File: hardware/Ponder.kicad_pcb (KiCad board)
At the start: 2 copper layers, 40 x 50 mm, 119 parts, among them J1 USB_C_Receptacle_USB2.0, J10 1.27 HDR, J11 2.54 SKT, J12 2.54 SKT, J2 2.54 HDR, J3 2.54 HDR, J4 2.54 HDR, J5 2.54 HDR, J6 2.54 HDR, J7 2.54 HDR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

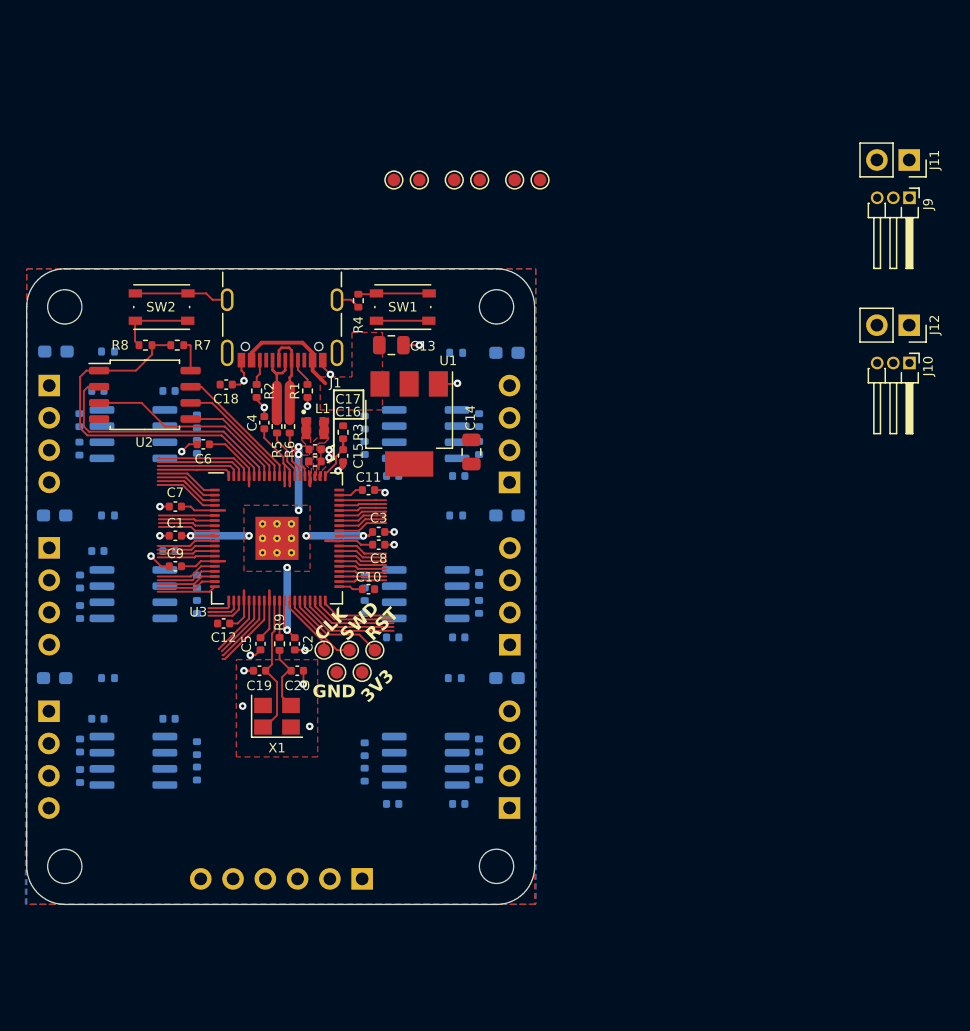
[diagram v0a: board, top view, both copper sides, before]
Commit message: Adding LEDs for power status
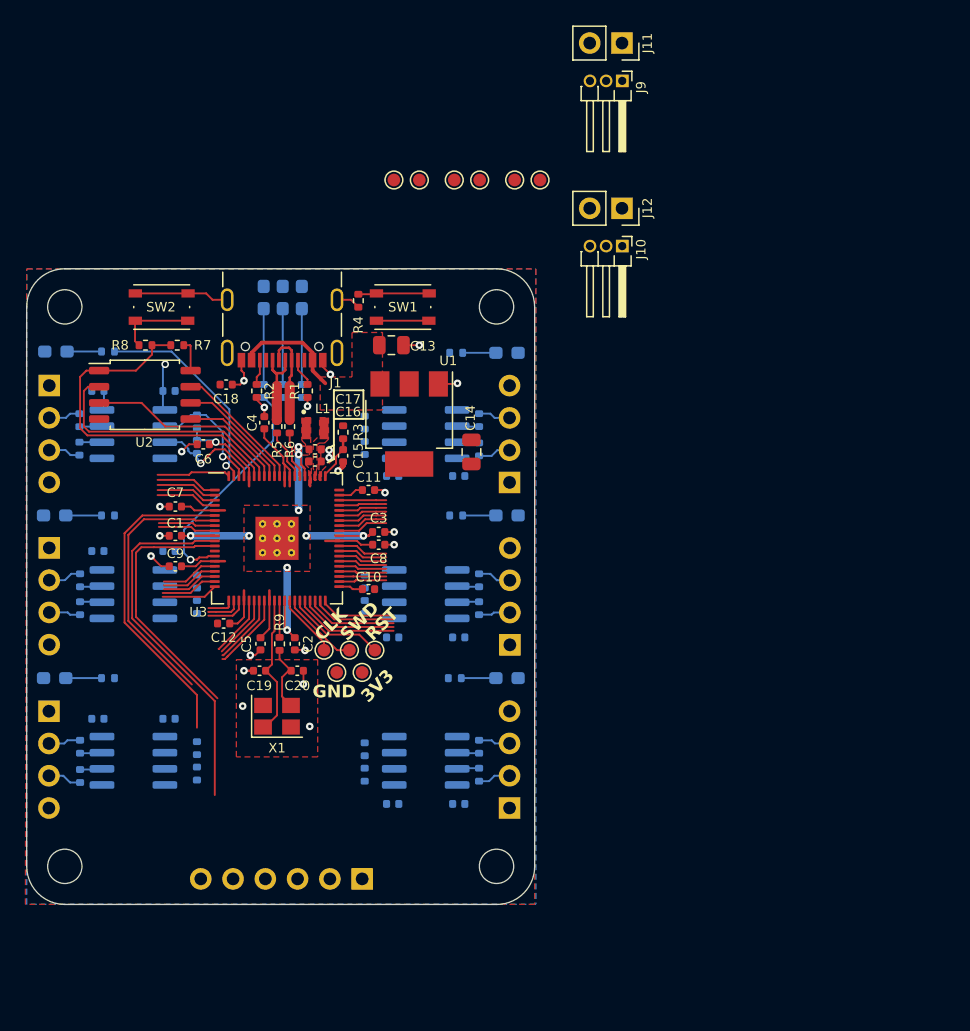
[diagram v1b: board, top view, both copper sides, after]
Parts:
- added D7: LED, LED_SMD:LED_0603_1608Metric_Pad1.05x0.95mm_HandSolder, B.Cu at (139.2, 75.2)
- added D8: LED, LED_SMD:LED_0603_1608Metric_Pad1.05x0.95mm_HandSolder, B.Cu at (140.8, 75.2)
- added D9: LED, LED_SMD:LED_0603_1608Metric_Pad1.05x0.95mm_HandSolder, B.Cu at (142.2, 75.2)
- added R40: 1k, Resistor_SMD:R_0402_1005Metric, B.Cu at (139.2, 82.6)
- added R41: 1k, Resistor_SMD:R_0402_1005Metric, B.Cu at (140.8, 82.6)
- added R42: 1k, Resistor_SMD:R_0402_1005Metric, B.Cu at (142.2, 82.6)
- moved J11 24.4 mm to (167.4, 55.2)
- moved J12 24.4 mm to (167.4, 68.2)
- moved J10 24.4 mm to (167.5, 71.2)
- moved J9 24.4 mm to (167.5, 58.2)
- moved R13 0.30 mm to (124.8, 99.7)
- moved R18 0.11 mm to (156.2, 99.7)
- moved R19 0.11 mm to (156.2, 97.5)
- moved R20 0.11 mm to (156.2, 87.2)
- moved R12 0.10 mm to (124.8, 97.5)
- moved R16 0.10 mm to (156.2, 112.8)
- moved R17 0.10 mm to (156.2, 110.6)
- moved R14 0.09 mm to (124.8, 110.6)
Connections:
- U3 pad 1: /GPIO4 -> /RP_UART1_TX
- U3 pad 11: /GPIO12 -> /RP_UART3_TX
- U3 pad 12: /GPIO13 -> /RP_UART3_RX
- U3 pad 13: /GPIO14 -> unconnected-(U3-GPIO14-Pad13)
- U3 pad 14: /GPIO15 -> /RP_PWR_LED
- U3 pad 16: /GPIO16 -> /RP_UART4_TX
- U3 pad 17: /GPIO17 -> /RP_UART4_RX
- U3 pad 18: /GPIO18 -> /RP_UART4_LED
- U3 pad 19: /GPIO19 -> /RP_UART5_LED
- U3 pad 2: /GPIO5 -> /RP_UART1_RX
- U3 pad 20: /GPIO20 -> /RP_UART5_TX
- U3 pad 21: /GPIO21 -> /RP_UART5_RX
- U3 pad 22: /GPIO22 -> unconnected-(U3-GPIO22-Pad22)
- U3 pad 23: /GPIO23 -> unconnected-(U3-GPIO23-Pad23)
- U3 pad 25: /GPIO24 -> /RP_SPI1-MISO_I2C0-SDA
- U3 pad 26: /GPIO25 -> /RP_SPI1-CSn_I2C0-SCL
- U3 pad 27: /GPIO26 -> /RP_SPI1-SCK_I2C1-SDA
- U3 pad 28: /GPIO27 -> /RP_SPI1-MOSI_I2C1-SCL
- U3 pad 3: /GPIO6 -> unconnected-(U3-GPIO6-Pad3)
- U3 pad 36: /GPIO28 -> unconnected-(U3-GPIO28-Pad36)
- U3 pad 37: /GPIO29 -> unconnected-(U3-GPIO29-Pad37)
- U3 pad 38: /GPIO30 -> unconnected-(U3-GPIO30-Pad38)
- U3 pad 39: /GPIO31 -> unconnected-(U3-GPIO31-Pad39)
- U3 pad 4: /GPIO7 -> unconnected-(U3-GPIO7-Pad4)
- U3 pad 40: /GPIO32 -> unconnected-(U3-GPIO32-Pad40)
- U3 pad 42: /GPIO33 -> unconnected-(U3-GPIO33-Pad42)
- U3 pad 43: /GPIO34 -> unconnected-(U3-GPIO34-Pad43)
- U3 pad 44: /GPIO35 -> unconnected-(U3-GPIO35-Pad44)
- U3 pad 45: /GPIO36 -> unconnected-(U3-GPIO36-Pad45)
- U3 pad 46: /GPIO37 -> unconnected-(U3-GPIO37-Pad46)
- U3 pad 47: /GPIO38 -> unconnected-(U3-GPIO38-Pad47)
- U3 pad 48: /GPIO39 -> unconnected-(U3-GPIO39-Pad48)
- U3 pad 6: /GPIO8 -> /RP_UART2_TX
- U3 pad 7: /GPIO9 -> /RP_UART2_RX
- U3 pad 77: /GPIO0 -> /RP_UART0_TX
- U3 pad 78: /GPIO1 -> /RP_UART0_RX
- U3 pad 79: /GPIO2 -> /RP_UART0_LED
- U3 pad 8: /GPIO10 -> /RP_UART2_LED
- U3 pad 80: /GPIO3 -> /RP_UART1_LED
- U3 pad 9: /GPIO11 -> /RP_UART3_LED
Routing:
- net /RP_UART3_TX: track 0.00 -> 28.7 mm
- net /RP_UART2_TX: track 0.00 -> 25.3 mm
- net /RP_UART2_RX: track 0.00 -> 21.2 mm
- net /RP_UART3_RX: track 0.00 -> 20.5 mm
- net /RP_PWR_LED: track 0.00 -> 18.2 mm, vias 0 -> 1
- net /RP_UART0_LED: track 0.00 -> 16.6 mm, vias 0 -> 1
- net /RP_UART0_RX: track 0.00 -> 9.64 mm, vias 0 -> 1
- net /RP_UART0_TX: track 0.00 -> 8.98 mm, vias 0 -> 1
- net unconnected-(U3-GPIO28-Pad36): track 0.00 -> 8.25 mm
- net /GPIO28: track 8.25 -> 0.00 mm
- net /GPIO0: track 7.73 -> 0.00 mm
- net unconnected-(U3-GPIO29-Pad37): track 0.00 -> 7.72 mm
- net /GPIO29: track 7.72 -> 0.00 mm
- net /GPIO1: track 7.20 -> 0.00 mm
- net unconnected-(U3-GPIO30-Pad38): track 0.00 -> 7.18 mm
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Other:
- board text added: "POWER"

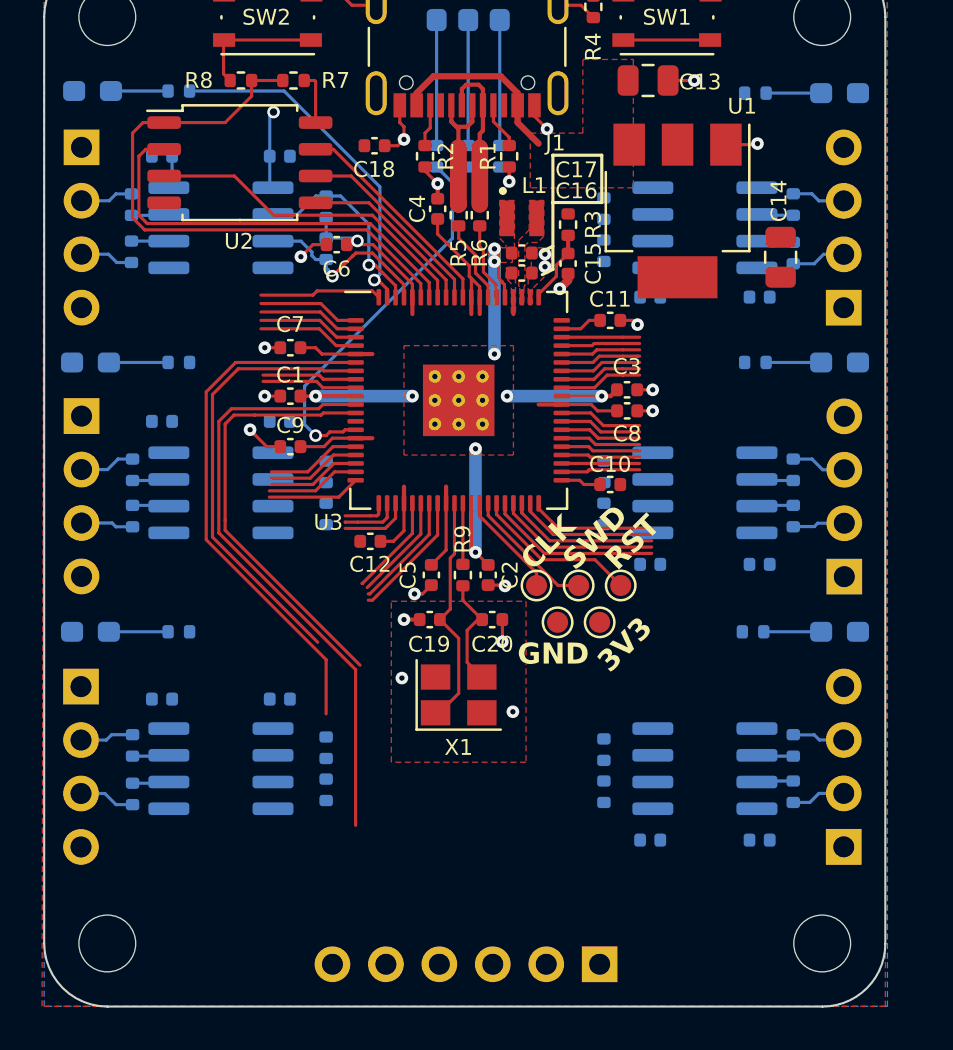
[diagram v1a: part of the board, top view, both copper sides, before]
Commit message: Tittivating connector legends
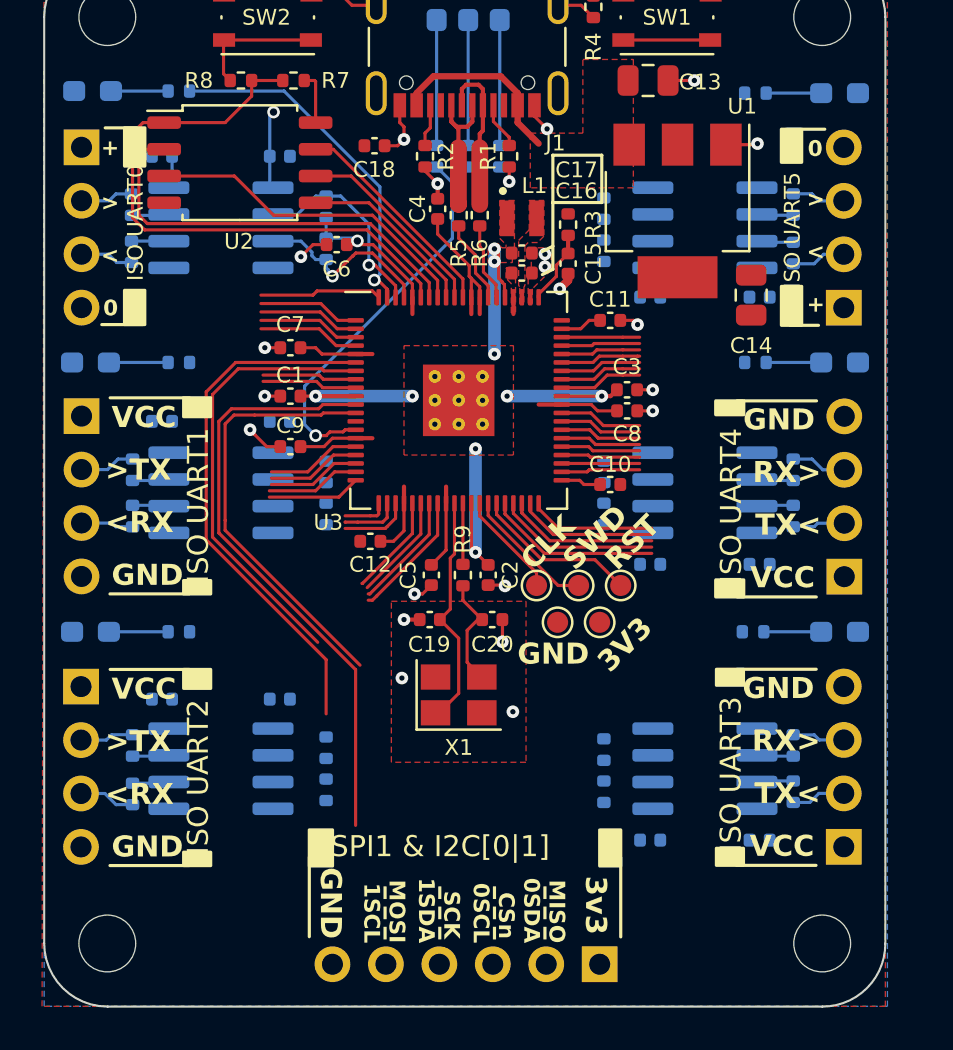
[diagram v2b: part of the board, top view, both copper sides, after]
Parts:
- moved C14 2.28 mm to (154.2, 89.2), turned to -90 degrees
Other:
- board text added: "+"
- board text added: "0"
- board text added: "0SCL"
- board text added: "0SDA"
- board text added: "1SCL"
- board text added: "1SDA"
- board text added: "3v3"
- board text added: "<"
- board text added: "<RX"
- board text added: ">"
- board text added: ">TX"
- board text added: "CSn"
- board text added: "ISO UART0"
- board text added: "ISO UART1"
- board text added: "ISO UART2"
- board text added: "ISO UART3"
- board text added: "ISO UART4"
- board text added: "ISO UART5"
- board text added: "MISO"
- board text added: "MOSI"
- board text added: "RX>"
- board text added: "SCK"
- board text added: "SPI1 & I2C[0|1]"
- board text added: "TX<"
- board text added: "VCC"

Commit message: Minor tweaks an bit of layout
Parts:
- moved R30 2.31 mm to (134.0, 110.4), turned to 90 degrees
- moved C14 2.02 mm to (153.1, 90.9), turned to 0 degrees
- moved R29 2.00 mm to (134.0, 112.7), turned to -90 degrees
- moved C12 0.71 mm to (136.2, 101.6), turned to -135 degrees
- moved C5 0.61 mm to (138.9, 103.1)
- moved C31 0.41 mm to (155.0, 101.9), turned to 0 degrees
- moved C32 0.41 mm to (155.0, 89.2), turned to 0 degrees
- moved C28 0.40 mm to (155.0, 115.1), turned to 0 degrees
- moved R20 0.10 mm to (156.3, 87.2)
- moved R21 0.10 mm to (156.3, 84.9)
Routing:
- net +3V3: track 45.2 -> 73.0 mm, vias 2 -> 12
- net /RP_SPI1-MISO_I2C0-SDA: track 4.81 -> 29.5 mm, vias 0 -> 1
- net /RP_SPI1-CSn_I2C0-SCL: track 5.06 -> 27.3 mm, vias 0 -> 1
- net /RP_SPI1-SCK_I2C1-SDA: track 5.55 -> 25.9 mm, vias 0 -> 1
- net /RP_SPI1-MOSI_I2C1-SCL: track 6.09 -> 24.0 mm
- net /RP_UART3_TX: track 28.7 -> 14.8 mm
- net /RP_UART1_TX: track 4.83 -> 16.1 mm, vias 0 -> 1
- net /RP_UART2_TX: track 25.3 -> 17.6 mm
- net /RP_UART1_RX: track 4.83 -> 11.8 mm, vias 0 -> 1
- net /RP_UART3_RX: track 20.5 -> 14.2 mm
- net /DUT1_VCC: track 0.00 -> 6.20 mm
- net /DUT2_VCC: track 0.00 -> 6.04 mm
- net /DUT3_VCC: track 0.00 -> 5.90 mm
- net /DUT4_VCC: track 0.00 -> 5.81 mm
- net /DUT5_VCC: track 0.00 -> 5.64 mm
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- added copper zone on B.Cu, net /DUT0_GND
- added copper zone on F.Cu, net /DUT0_VCC
- added copper zone on B.Cu, net /DUT1_GND
- added copper zone on F.Cu, net /DUT1_VCC
- added copper zone on B.Cu, net /DUT2_GND
- added copper zone on F.Cu, net /DUT2_VCC
- added copper zone on B.Cu, net /DUT3_GND
- added copper zone on F.Cu, net /DUT3_VCC
- added copper zone on B.Cu, net /DUT4_GND
- added copper zone on F.Cu, net /DUT4_VCC
- added copper zone on B.Cu, net /DUT5_GND
- added copper zone on F.Cu, net /DUT5_VCC
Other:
- board text added: "SCL0"
- board text added: "SCL1"
- board text added: "SDA0"
- board text added: "SDA1"
- board text removed: "0SCL"
- board text removed: "0SDA"
- board text removed: "1SCL"
- board text removed: "1SDA"

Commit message: First pass layout
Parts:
- removed J12: 2.54 SKT, Connector_PinSocket_2.54mm:PinSocket_1x02_P2.54mm_Vertical
- removed the TP1 at (151.5, 66.0)
- removed the TP2 at (156.2, 66.0)
- removed the TP3 at (149.5, 66.0)
- removed the TP4 at (154.2, 66.0)
- removed the TP5 at (159.0, 66.0)
- added D10: NSR0530HT1G, Diode_SMD:D_SOD-323, F.Cu at (127.4, 78.8)
- added R43: 10k, Resistor_SMD:R_0402_1005Metric, F.Cu at (123.0, 79.6)
- added R44: 10k, Resistor_SMD:R_0402_1005Metric, F.Cu at (125.8, 79.4)
- added TP10: TestPoint, TestPoint:TestPoint_Pad_D1.0mm, F.Cu at (148.3, 92.2)
- added TP11: TestPoint, TestPoint:TestPoint_Pad_D1.0mm, F.Cu at (150.3, 91.7)
- added TP12: TestPoint, TestPoint:TestPoint_Pad_D1.0mm, F.Cu at (146.9, 96.1)
- added TP7: TestPoint, TestPoint:TestPoint_Pad_D1.0mm, F.Cu at (129.8, 90.6)
- added TP8: TestPoint, TestPoint:TestPoint_Pad_D1.0mm, F.Cu at (131.6, 89.6)
- added TP9: TestPoint, TestPoint:TestPoint_Pad_D1.0mm, F.Cu at (129.8, 93.5)
- C16, C17: footprint Capacitor_SMD:C_0402_1005Metric -> Ponder:C_0402_1005Metric_small_pads
- J10: value 1.27 HDR -> 2.54 SKT; footprint Connector_PinHeader_1.27mm:PinHeader_1x03_P1.27mm_Horizontal -> Ponder:M208890245; moved to B.Cu
- J11: value 2.54 SKT -> 2.54 HDR; footprint Connector_PinSocket_2.54mm:PinSocket_1x02_P2.54mm_Vertical -> Connector_PinHeader_2.54mm:PinHeader_1x04_P2.54mm_Vertical_SMD_Pin1Left
- J9: footprint Connector_PinHeader_1.27mm:PinHeader_1x03_P1.27mm_Horizontal -> Connector_PinHeader_1.27mm:PinHeader_1x03_P1.27mm_Vertical; moved to B.Cu
- R7: value OMIT -> 10k
- SW1, SW2: value SW_Push -> 434133025816
- U2: value W25Q128JVS -> W25Q64JVXGIQ_TR; footprint Package_SO:SOIC-8_5.23x5.23mm_P1.27mm -> Ponder:SON80P400X400X50-9N
- moved J11 65.6 mm to (131.6, 110.1), turned to 0 degrees
- moved TP6 38.5 mm to (129.8, 88.6), turned to 0 degrees
- moved J9 27.7 mm to (146.9, 76.8), turned to 180 degrees
- moved J10 15.8 mm to (151.8, 73.2), turned to 180 degrees
- moved R8 4.41 mm to (127.4, 75.4), turned to -90 degrees
- moved U2 4.01 mm to (133.8, 83.6)
- moved G1 2.91 mm to (140.6, 112.0)
- moved C18 2.55 mm to (134.6, 80.2), turned to 90 degrees
- moved R7 2.48 mm to (130.0, 79.4), turned to -90 degrees
- moved R35 0.90 mm to (155.3, 79.6)
- moved C10 0.40 mm to (147.5, 98.6)
- moved R4 0.20 mm to (146.7, 75.3)
- moved R27 0.10 mm to (134.0, 97.7)
- renumbered TP7 to TP1, TP8 to TP2, TP9 to TP3, TP10 to TP4, TP11 to TP5
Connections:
- J10 pad 1: +3V3 -> GND
- J11 pad 1: /VOUT1_SELECT -> /GPIO15
- J11 pad 2: GND -> /GPIO16
- J9 pad 2: /VOUT2_SELECT -> /VOUT1_SELECT
- R8 pad 1: /QSPI_SS -> Net-(R43-Pad2)
- R8 pad 2: /~{USB_BOOT} -> Net-(D10-K)
- SW2 pad 1: GND -> Net-(R43-Pad2)
- SW2 pad 2: /~{USB_BOOT} -> GND
- TP6 pad 1: +1V1 -> /GPIO5
- U3 pad 1: /RP_UART1_TX -> /RP_PWR_LED
- U3 pad 11: /RP_UART3_TX -> unconnected-(U3-GPIO12-Pad11)
- U3 pad 12: /RP_UART3_RX -> unconnected-(U3-GPIO13-Pad12)
- U3 pad 14: /RP_PWR_LED -> /GPIO15
- U3 pad 16: /RP_UART4_TX -> /GPIO16
- U3 pad 17: /RP_UART4_RX -> /GPIO17
- U3 pad 18: /RP_UART4_LED -> /GPIO18
- U3 pad 19: /RP_UART5_LED -> /RP_UART2_LED
- U3 pad 2: /RP_UART1_RX -> /GPIO5
- U3 pad 20: /RP_UART5_TX -> /RP_UART1_TX
- U3 pad 21: /RP_UART5_RX -> /RP_UART1_RX
- U3 pad 22: unconnected-(U3-GPIO22-Pad22) -> /RP_UART2_RX
- U3 pad 23: unconnected-(U3-GPIO23-Pad23) -> /RP_UART2_TX
- U3 pad 3: unconnected-(U3-GPIO6-Pad3) -> /GPIO6
- U3 pad 36: unconnected-(U3-GPIO28-Pad36) -> /RP_UART3_RX
- U3 pad 37: unconnected-(U3-GPIO29-Pad37) -> /RP_UART3_TX
- U3 pad 38: unconnected-(U3-GPIO30-Pad38) -> /RP_UART3_LED
- U3 pad 4: unconnected-(U3-GPIO7-Pad4) -> /GPIO7
- U3 pad 40: unconnected-(U3-GPIO32-Pad40) -> /RP_UART4_RX
- U3 pad 42: unconnected-(U3-GPIO33-Pad42) -> /RP_UART4_TX
- U3 pad 43: unconnected-(U3-GPIO34-Pad43) -> /RP_UART4_LED
- U3 pad 54: /GPIO43_ADC3 -> unconnected-(U3-GPIO43_ADC3-Pad54)
- U3 pad 55: /GPIO44_ADC4 -> unconnected-(U3-GPIO44_ADC4-Pad55)
- U3 pad 56: /GPIO45_ADC5 -> /RP_UART5_LED
- U3 pad 57: /GPIO46_ADC6 -> /RP_UART5_RX
- U3 pad 58: /GPIO47_ADC7 -> /RP_UART5_TX
- U3 pad 6: /RP_UART2_TX -> /RP_UART1_LED
- U3 pad 7: /RP_UART2_RX -> /GPIO9
- U3 pad 8: /RP_UART2_LED -> unconnected-(U3-GPIO10-Pad8)
- U3 pad 80: /RP_UART1_LED -> /USR_SW
- U3 pad 9: /RP_UART3_LED -> unconnected-(U3-GPIO11-Pad9)
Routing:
- net /RUN: track 12.0 -> 46.6 mm, vias 0 -> 3
- net /GPIO18: track 0.00 -> 20.5 mm
- net /GPIO17: track 0.00 -> 18.5 mm
- net /GPIO16: track 0.00 -> 17.6 mm, vias 0 -> 2
- net /USR_SW: track 0.00 -> 17.1 mm
- net /GPIO15: track 0.00 -> 15.5 mm, vias 0 -> 2
- net /RP_UART5_LED: track 4.48 -> 19.4 mm, vias 0 -> 1
- net Net-(R43-Pad2): track 0.00 -> 13.7 mm
- net /RP_UART1_TX: track 16.1 -> 6.21 mm
- net GND: track 31.2 -> 41.0 mm, vias 23 -> 29
- net /RP_UART3_LED: track 4.53 -> 13.6 mm, vias 0 -> 1
- net unconnected-(U3-GPIO28-Pad36): track 8.25 -> 0.00 mm
- net /QSPI_SS: track 28.3 -> 20.3 mm
- net unconnected-(U3-GPIO29-Pad37): track 7.72 -> 0.00 mm
- net /RP_UART2_LED: track 4.49 -> 11.9 mm, vias 0 -> 1
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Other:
- board text added: "40"
- board text added: "41"
- board text added: "42"
- board text added: "5"
- board text added: "6"
- board text added: "7"
- board text added: "9"
- board text added: "SEL"
- board text added: "USB"

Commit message: Silk tittivating
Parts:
- added J12: 1.27 HDR, Connector_PinHeader_1.27mm:PinHeader_1x03_P1.27mm_Vertical, F.Cu at (136.6, 113.6)
- added J13: 1.27 HDR, Connector_PinHeader_1.27mm:PinHeader_1x03_P1.27mm_Vertical, F.Cu at (139.7, 113.5)
- added J14: 1.27 HDR, Connector_PinHeader_1.27mm:PinHeader_1x03_P1.27mm_Vertical, F.Cu at (142.8, 113.6)
- added J15: 1.27 HDR, Connector_PinHeader_1.27mm:PinHeader_1x03_P1.27mm_Vertical, F.Cu at (145.9, 113.6)
- added R45: 10k, Resistor_SMD:R_0402_1005Metric, B.Cu at (144.6, 115.4)
- added R46: 10k, Resistor_SMD:R_0402_1005Metric, B.Cu at (141.4, 115.4)
- added R47: 10k, Resistor_SMD:R_0402_1005Metric, B.Cu at (135.2, 115.4)
- added R48: 10k, Resistor_SMD:R_0402_1005Metric, B.Cu at (138.2, 115.4)
- J8: moved to F.Cu
- moved G1 36.8 mm to (130.6, 76.7)
- moved J8 12.0 mm to (135.0, 120.8)
- moved G2 2.90 mm to (140.6, 96.5)
- moved R32 0.30 mm to (147.5, 110.8)
- moved R33 0.30 mm to (147.5, 112.8)
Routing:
- net /RP_SPI1-MOSI_I2C1-SCL: track 23.5 -> 36.8 mm
- net /RP_SPI1-SCK_I2C1-SDA: track 25.8 -> 34.3 mm, vias 1 -> 0
- net /RP_SPI1-CSn_I2C0-SCL: track 28.0 -> 31.9 mm, vias 1 -> 0
- net +3V3: track 73.6 -> 71.6 mm
- net Net-(J13-Pin_2): track 0.00 -> 1.58 mm
- net /RP_UART3_RX: track 19.3 -> 17.8 mm
- net Net-(J14-Pin_2): track 0.00 -> 1.42 mm
- net Net-(J12-Pin_2): track 0.00 -> 1.37 mm
- net Net-(J15-Pin_2): track 0.00 -> 1.32 mm
- net /RP_UART3_TX: track 17.1 -> 16.0 mm
- net /RP_SPI1-MISO_I2C0-SDA: track 29.5 -> 30.1 mm, vias 1 -> 0
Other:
- board text added: "15"
- board text added: "16"
- board text added: "17"
- board text added: "18"
- board text added: "Dn"
- board text added: "Pull Rs"
- board text added: "SPI & I2C"
- board text added: "Up"
- board text added: "VOUT"
- board text removed: "SPI1 & I2C[0|1]"
